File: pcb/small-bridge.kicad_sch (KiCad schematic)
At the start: 3 parts, among them Q15 AON7544, Q16 AON7544

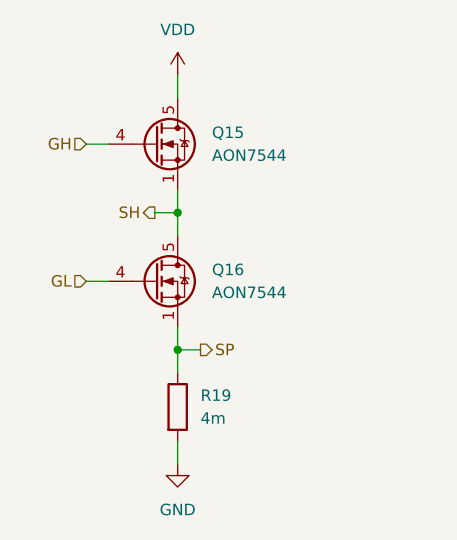
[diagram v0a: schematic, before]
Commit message: Finish rough layout
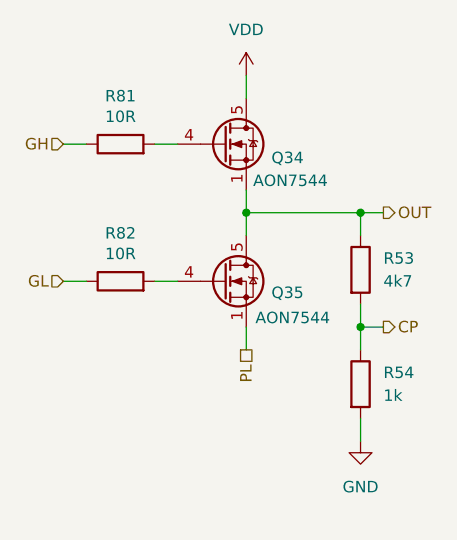
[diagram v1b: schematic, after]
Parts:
- removed Q15, Q16: AON7544, User_Footprints:DFN3x3A_8L_EP1_P, symbol User_Symbols:AON7544
- removed R19: 4m, Resistor_SMD:R_2512_6332Metric, symbol Device:R
- added Q34, Q35: AON7544, User_Footprints:DFN3x3A_8L_EP1_P, symbol User_Symbols:AON7544
- added R53: 4k7, Resistor_SMD:R_0402_1005Metric, symbol Device:R
- added R54: 1k, Resistor_SMD:R_0402_1005Metric, symbol Device:R
- added R81, R82: 10R, Resistor_SMD:R_0402_1005Metric, symbol Device:R
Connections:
- net GH: now also R81.1
- net GL: now also R82.1
- net GND: now also R54.2
- net VDD: now also Q34.5 (D), Q34.6 (D), Q34.7 (D), Q34.8 (D)
- new net: Q34.4 (G), R81.2
- new net: Q35.4 (G), R82.2
- new net CP: R53.2, R54.1
- new net OUT: Q34.1 (S), Q34.2 (S), Q34.3 (S), Q35.5 (D), Q35.6 (D), Q35.7 (D), Q35.8 (D), R53.1
- new net PL: Q35.1 (S), Q35.2 (S), Q35.3 (S)

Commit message: Finish pcb
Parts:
- R81, R82: LCSC C25139 -> C25077
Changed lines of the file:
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@@
 			)
 		)
-		(property "LCSC" "C25139"
+		(property "LCSC" "C25077"
 			(at 57.15 58.42 90)
 			(effects
@@
 			)
 		)
-		(property "LCSC" "C25139"
+		(property "LCSC" "C25077"
 			(at 57.15 73.66 90)
 			(effects
